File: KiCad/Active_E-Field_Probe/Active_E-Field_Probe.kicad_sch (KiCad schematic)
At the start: 3 parts

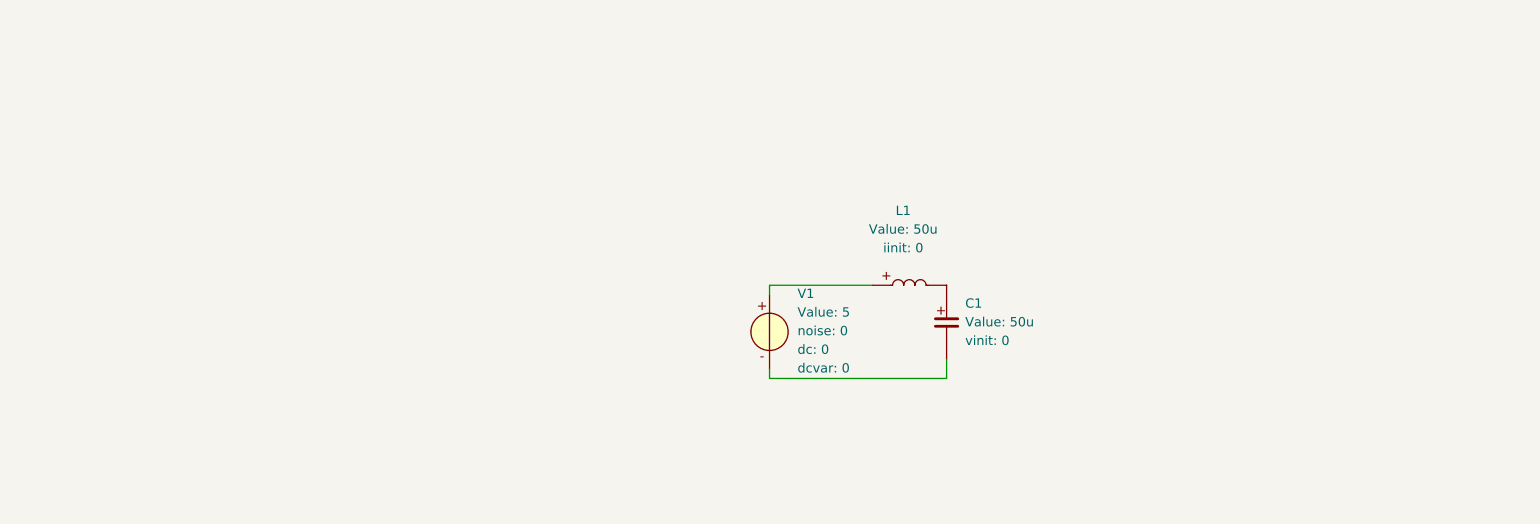
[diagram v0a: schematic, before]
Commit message: nullor implementation v1
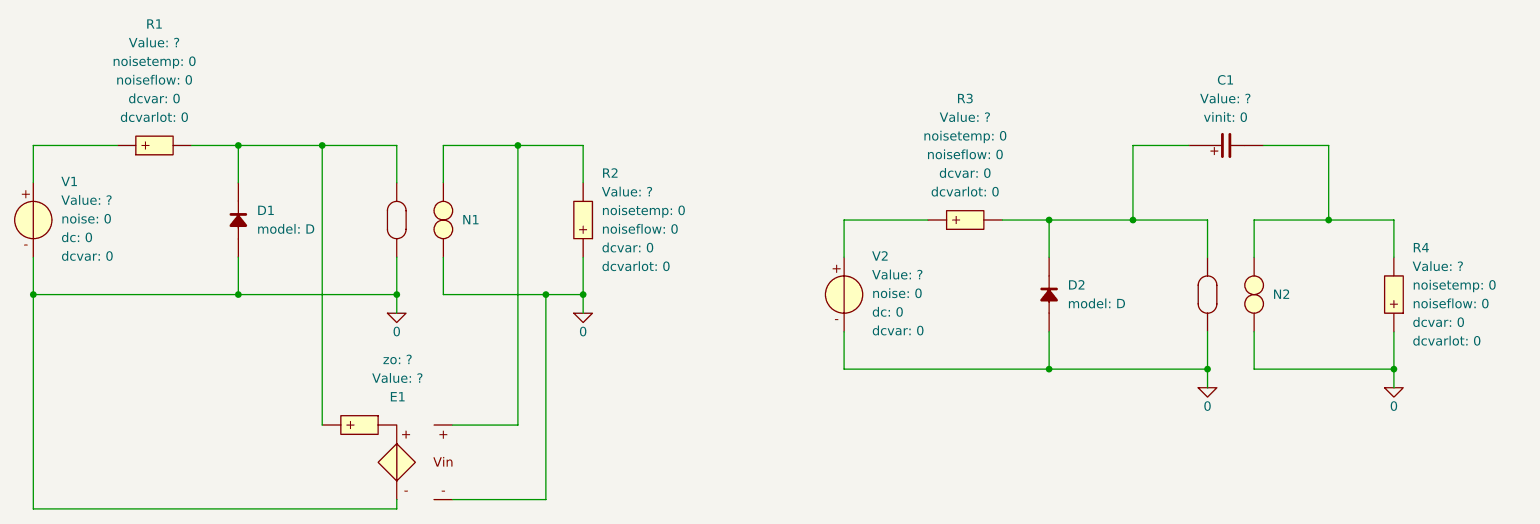
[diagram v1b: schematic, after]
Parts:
- removed L1: 50u, symbol SLiCAP:L
- added D1, D2: ~, symbol SLiCAP:D
- added E1: ?, symbol SLiCAP:EZ
- added N1, N2: ~, symbol SLiCAP:N
- added R1, R2, R3, R4: ?, symbol SLiCAP:R
- added V2: ?, symbol SLiCAP:V
- C1: value 50u -> ?
- V1: value 5 -> ?
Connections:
- net at C1.1: now also D2.2, N2.3 (inp), R3.2
- net at C1.2: now also N2.1 (outP), R4.2; no longer V1.2 (n)
- net at V1.1 (p): now also R1.1
- new net: E1.3 (inp), N1.1 (outP), R2.2
- new net: R3.1, V2.1 (p)
- new net: D1.2, E1.1 (outP), N1.3 (inp), R1.2
- new net 0: D1.1, D2.1, E1.2 (outN), E1.4 (inN), N1.2 (outN), N1.4 (inN), N2.2 (outN), N2.4 (inN), R2.1, R4.1, V1.2 (n), V2.2 (n)
